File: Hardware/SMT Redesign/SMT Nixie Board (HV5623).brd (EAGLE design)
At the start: 167.6 x 43.4 mm, 43 parts, among them J4 1, T0 IN-14(R), T1 IN-14(R), T2 IN-14(R), T3 IN-14(R), T4 IN-14(R), T5 IN-14(R), T6 IN-14(R), T7 IN-14(R), U6 HV5623K7-G, U7 HV5623K7-G, U8 HV5623K7-G

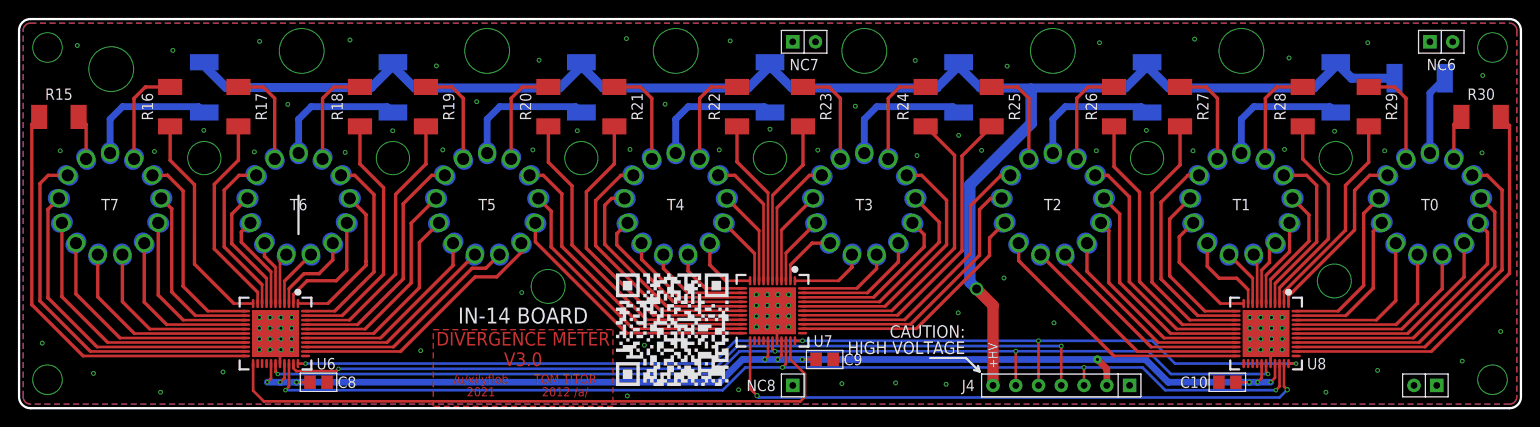
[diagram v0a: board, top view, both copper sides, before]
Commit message: Component numbering fix
There was a gap from U3 to U5, shifted U5 onwards down one (eg to U4).

Was also playing the with DR for JLCPCB, some pads etc may be wonky because of this.
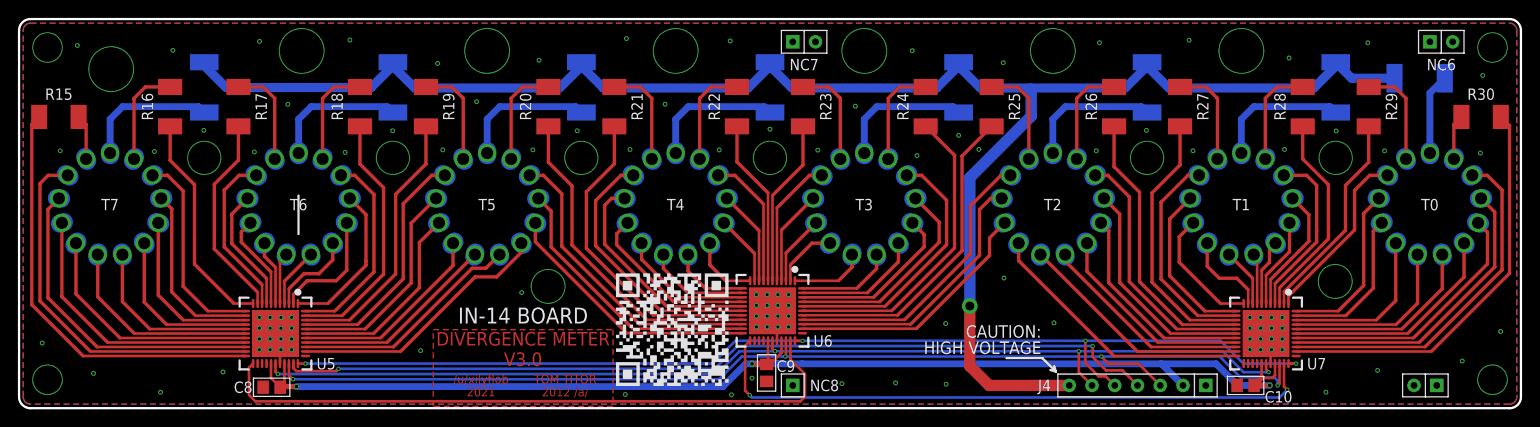
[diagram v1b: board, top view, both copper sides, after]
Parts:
- removed U8: HV5623K7-G, My Imported Components:WQFN-44
- added U5: HV5623K7-G, My Imported Components:WQFN-44
- moved U6 55.5 mm to (84.1, 10.9)
- moved U7 55.2 mm to (139.2, 8.33)
- moved J4 8.51 mm to (124.8, 2.54)
- moved C9 6.65 mm to (83.4, 3.94), turned to 270 degrees
- moved C8 5.26 mm to (28.2, 2.34), turned to 180 degrees
- moved C10 2.06 mm to (136.9, 2.54)
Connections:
- net !BL!: now also U5.33; no longer U8.33
- net !LE!: now also U5.31; no longer U8.31
- net +5V: now also U5.27, U5.30; no longer U8.27, U8.30
- net CLK: now also U5.28; no longer U8.28
- net DIN: now also U5.32; no longer U6.32
- net GND: now also U5.29, U5.P$1, U5.P$10, U5.P$11, U5.P$12, U5.P$13, U5.P$14, U5.P$15, U5.P$16, U5.P$2, U5.P$3, U5.P$4, U5.P$5, U5.P$6, U5.P$7, U5.P$8, U5.P$9, U5.TP; no longer U8.29, U8.P$1, U8.P$10, U8.P$11, U8.P$12, U8.P$13, U8.P$14, U8.P$15, U8.P$16, U8.P$2, U8.P$3, U8.P$4, U8.P$5, U8.P$6, U8.P$7, U8.P$8, U8.P$9, U8.TP
- net U5-T0K0: now also U5.21; no longer U6.21
- net U5-T0K1: now also U5.12; no longer U6.12
- net U5-T0K2: now also U5.13; no longer U6.13
- net U5-T0K3: now also U5.14; no longer U6.14
- net U5-T0K4: now also U5.15; no longer U6.15
- net U5-T0K5: now also U5.16; no longer U6.16
- net U5-T0K6: now also U5.17; no longer U6.17
- net U5-T0K7: now also U5.18; no longer U6.18
- net U5-T0K8: now also U5.19; no longer U6.19
- net U5-T0K9: now also U5.20; no longer U6.20
- net U5-T0LDP: now also U5.11; no longer U6.11
- net U5-T0RDP: now also U5.22; no longer U6.22
- net U5-T1K0: now also U5.9; no longer U6.9
- net U5-T1K1: now also U5.44; no longer U6.44
- net U5-T1K2: now also U5.1; no longer U6.1
- net U5-T1K3: now also U5.2; no longer U6.2
- net U5-T1K4: now also U5.3; no longer U6.3
- net U5-T1K5: now also U5.4; no longer U6.4
- net U5-T1K6: now also U5.5; no longer U6.5
- net U5-T1K7: now also U5.6; no longer U6.6
- net U5-T1K8: now also U5.7; no longer U6.7
- net U5-T1K9: now also U5.8; no longer U6.8
- net U5-T1LDP: now also U5.43; no longer U6.43
- net U5-T1RDP: now also U5.10; no longer U6.10
- net U5-T2K0: now also U5.41; no longer U6.41
- net U5-T2K4: now also U5.35; no longer U6.35
- net U5-T2K5: now also U5.36; no longer U6.36
- net U5-T2K6: now also U5.37; no longer U6.37
- net U5-T2K7: now also U5.38; no longer U6.38
- net U5-T2K8: now also U5.39; no longer U6.39
- net U5-T2K9: now also U5.40; no longer U6.40
- net U5-T2RDP: now also U5.42; no longer U6.42
- net U5-U6: now also U5.23, U6.32; no longer U6.23, U7.32
- net U6-T2K1: now also U6.20; no longer U7.20
- net U6-T2K2: now also U6.21; no longer U7.21
- net U6-T2K3: now also U6.22; no longer U7.22
- net U6-T2LDP: now also U6.19; no longer U7.19
- net U6-T3K0: now also U6.17; no longer U7.17
- net U6-T3K1: now also U6.8; no longer U7.8
- net U6-T3K2: now also U6.9; no longer U7.9
- net U6-T3K3: now also U6.10; no longer U7.10
- net U6-T3K4: now also U6.11; no longer U7.11
- net U6-T3K5: now also U6.12; no longer U7.12
- net U6-T3K6: now also U6.13; no longer U7.13
- net U6-T3K7: now also U6.14; no longer U7.14
- net U6-T3K8: now also U6.15; no longer U7.15
- net U6-T3K9: now also U6.16; no longer U7.16
- net U6-T3LDP: now also U6.7; no longer U7.7
- net U6-T3RDP: now also U6.18; no longer U7.18
- net U6-T4K0: now also U6.5; no longer U7.5
- net U6-T4K1: now also U6.40; no longer U7.40
- net U6-T4K2: now also U6.41; no longer U7.41
- net U6-T4K3: now also U6.42; no longer U7.42
- net U6-T4K4: now also U6.43; no longer U7.43
- net U6-T4K5: now also U6.44; no longer U7.44
- net U6-T4K6: now also U6.1; no longer U7.1
- net U6-T4K7: now also U6.2; no longer U7.2
- net U6-T4K8: now also U6.3; no longer U7.3
- net U6-T4K9: now also U6.4; no longer U7.4
- net U6-T4LDP: now also U6.39; no longer U7.39
- net U6-T4RDP: now also U6.6; no longer U7.6
- net U6-T5K0: now also U6.37; no longer U7.37
- net U6-T5K8: now also U6.35; no longer U7.35
- net U6-T5K9: now also U6.36; no longer U7.36
- net U6-T5RDP: now also U6.38; no longer U7.38
- net U6-U7: now also U6.23, U7.32; no longer U7.23, U8.32
- net U7-T5K1: now also U7.16; no longer U8.16
- net U7-T5K2: now also U7.17; no longer U8.17
- net U7-T5K3: now also U7.18; no longer U8.18
- net U7-T5K4: now also U7.19; no longer U8.19
- net U7-T5K5: now also U7.20; no longer U8.20
- net U7-T5K6: now also U7.21; no longer U8.21
- net U7-T5K7: now also U7.22; no longer U8.22
- net U7-T5LDP: now also U7.15; no longer U8.15
- net U7-T6K0: now also U7.13; no longer U8.13
- net U7-T6K1: now also U7.4; no longer U8.4
- net U7-T6K2: now also U7.5; no longer U8.5
- net U7-T6K3: now also U7.6; no longer U8.6
- net U7-T6K4: now also U7.7; no longer U8.7
- net U7-T6K5: now also U7.8; no longer U8.8
- net U7-T6K6: now also U7.9; no longer U8.9
- net U7-T6K7: now also U7.10; no longer U8.10
- net U7-T6K8: now also U7.11; no longer U8.11
- net U7-T6K9: now also U7.12; no longer U8.12
- net U7-T6LDP: now also U7.3; no longer U8.3
- net U7-T6RDP: now also U7.14; no longer U8.14
- net U7-T7K0: now also U7.1; no longer U8.1
- net U7-T7K1: now also U7.36; no longer U8.36
- net U7-T7K2: now also U7.37; no longer U8.37
- net U7-T7K3: now also U7.38; no longer U8.38
- net U7-T7K4: now also U7.39; no longer U8.39
- net U7-T7K5: now also U7.40; no longer U8.40
- net U7-T7K6: now also U7.41; no longer U8.41
- net U7-T7K7: now also U7.42; no longer U8.42
- net U7-T7K8: now also U7.43; no longer U8.43
- net U7-T7K9: now also U7.44; no longer U8.44
- net U7-T7LDP: now also U7.35; no longer U8.35
- net U7-T7RDP: now also U7.2; no longer U8.2
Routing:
- net +HV: track 186.7 -> 195.5 mm
- net DIN: track 91.9 -> 98.6 mm
- net !LE!: track 124.1 -> 126.8 mm
- net !BL!: track 120.2 -> 122.0 mm
- net +5V: track 135.5 -> 137.2 mm, vias 10 -> 3
- net U5-U6: track 72.3 -> 73.2 mm
- net U6-U7: track 69.1 -> 70.1 mm
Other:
- board text removed: "+HV"
